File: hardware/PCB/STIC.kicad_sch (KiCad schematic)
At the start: 18 parts, among them J1 22-03-5035, J2 53047-0510, J3 53047-0310, J4 3 way molex cable, J5 Conn_01x02, U1 XIAO_BLE, U2 RM3100_Breakout, U3 OLED1_3_GND1

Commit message: More work on the BOM
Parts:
- added LASER1: Egismos Laser Module 2, symbol Graphic:SYM_LASER_Large
- U1: Manufacturer_Name (none) -> Seeed
- U2: Manufacturer_Part_Number (none) -> https://www.aliexpress.com/item/1005001698153630.html
- U3: Manufacturer_Part_Number (none) -> https://www.aliexpress.com/item/32830144222.html

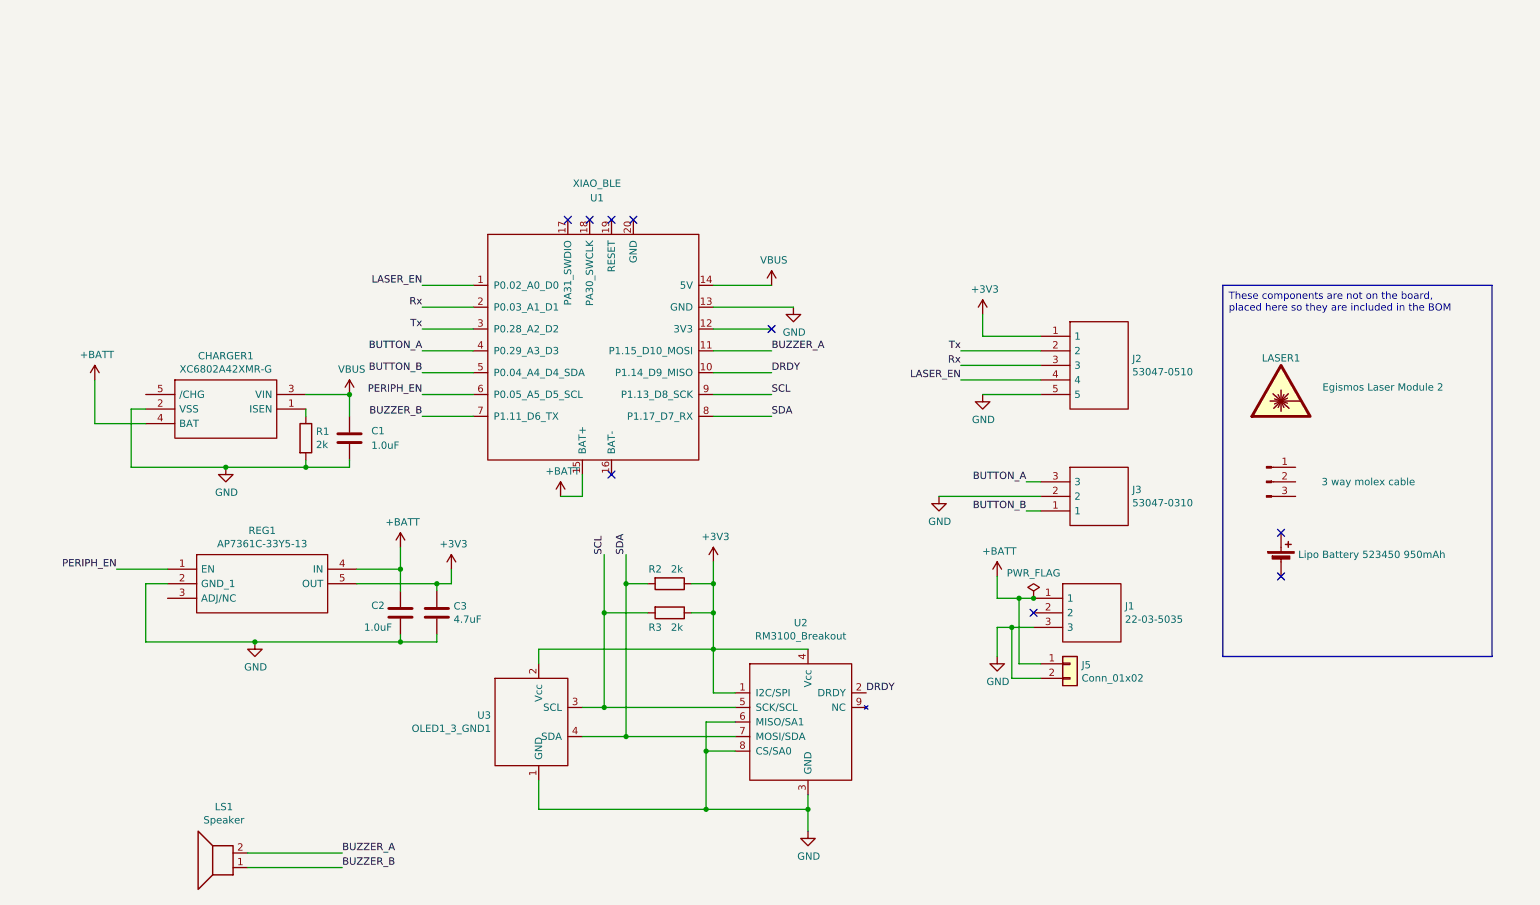
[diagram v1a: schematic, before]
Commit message: Update to Kicad v8.
Make board 5mm shorter and add SMD components
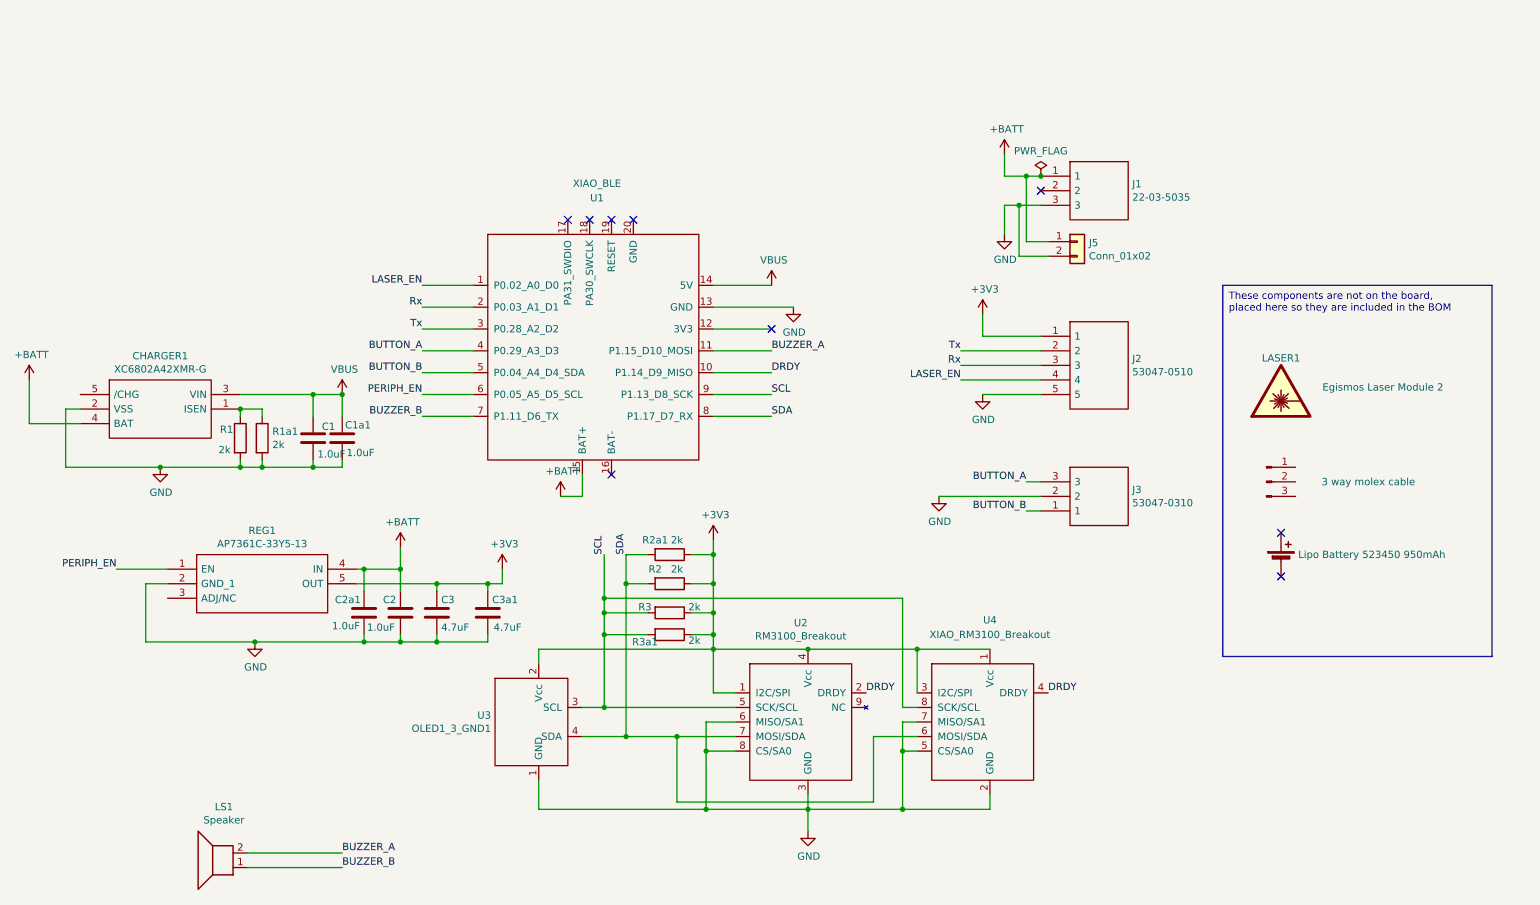
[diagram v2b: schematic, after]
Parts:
- added C1a1, C2a1: 1.0uF, Capacitor_SMD:C_0603_1608Metric, symbol Device:C
- added C3a1: 4.7uF, Capacitor_SMD:C_0603_1608Metric, symbol Device:C
- added R1a1, R2a1, R3a1: 2k, Resistor_SMD:R_0603_1608Metric, symbol Device:R
- added U4: XIAO_RM3100_Breakout, STIC:RM3100_red, symbol STIC-rescue:RM3100_red
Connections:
- net +3V3: now also C3a1.1, R2a1.1, R3a1.1, U4.1 (Vcc), U4.3 (I2C/SPI)
- net +BATT: now also C2a1.1
- net DRDY: now also U4.4 (DRDY)
- net GND: now also C1a1.2, C2a1.2, C3a1.2, R1a1.2, U4.2 (GND), U4.5 (CS/SA0), U4.7 (MISO/SA1)
- net SCL: now also R3a1.2, U4.8 (SCK/SCL)
- net SDA: now also R2a1.2, U4.6 (MOSI/SDA)
- net VBUS: now also C1a1.1
- net at CHARGER1.1 (ISEN), R1.1: now also R1a1.1
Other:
- moved on the sheet: C1, CHARGER1, J1, J5, R1

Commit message: Revert "Update to Kicad v8."
This reverts commit 377b650fb4ed8263ac52fe62880b4f170809fcf5.
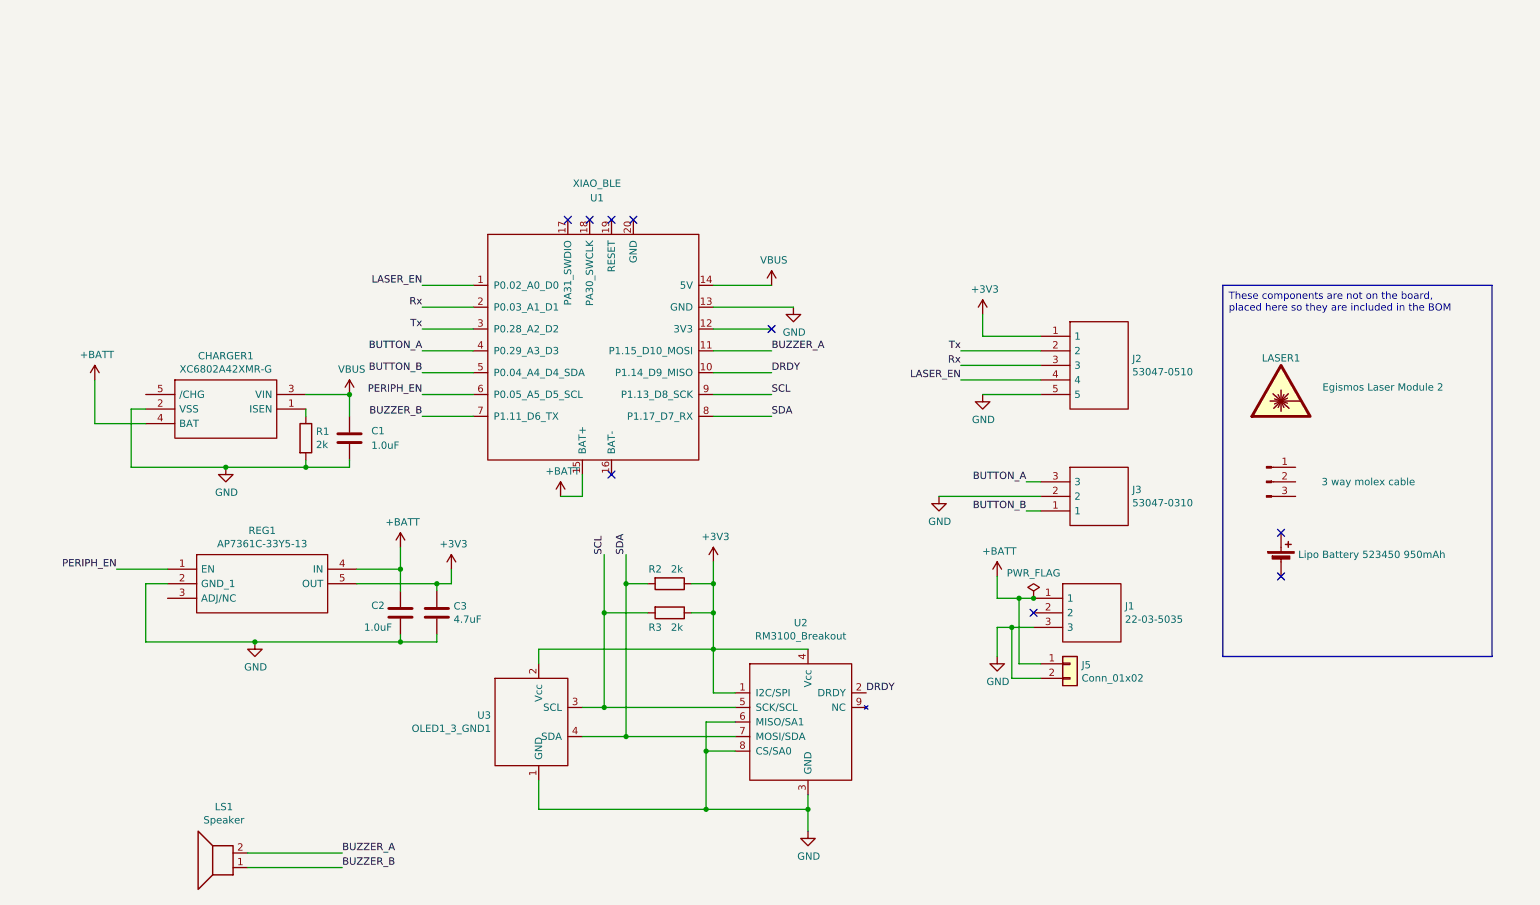
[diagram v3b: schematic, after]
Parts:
- removed C1a1, C2a1: 1.0uF, Capacitor_SMD:C_0603_1608Metric, symbol Device:C
- removed C3a1: 4.7uF, Capacitor_SMD:C_0603_1608Metric, symbol Device:C
- removed R1a1, R2a1, R3a1: 2k, Resistor_SMD:R_0603_1608Metric, symbol Device:R
- removed U4: XIAO_RM3100_Breakout, STIC:RM3100_red, symbol STIC-rescue:RM3100_red
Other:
- moved on the sheet: C1, CHARGER1, J1, J5, R1

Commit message: Merge 6.2 into main
Makes the case 5mm shorter
Also sets up "layout" system for various hardware

# Conflicts:
#	firmware/calibrate.py
#	firmware/debug.py
#	firmware/docs/source/conf.py
#	firmware/installer/installer.py
#	firmware/layouts.py
#	firmware/pins.py
#	firmware/requirements.txt
#	firmware/utils.py
#	firmware/version.py
#	firmware/versions/display128x64.py
#	hardware/Button/Button.kicad_pro
#	hardware/PCB/STIC.kicad_pcb
#	hardware/PCB/STIC.kicad_prl
#	hardware/PCB/STIC.kicad_pro
#	hardware/PCB/STIC.kicad_sch
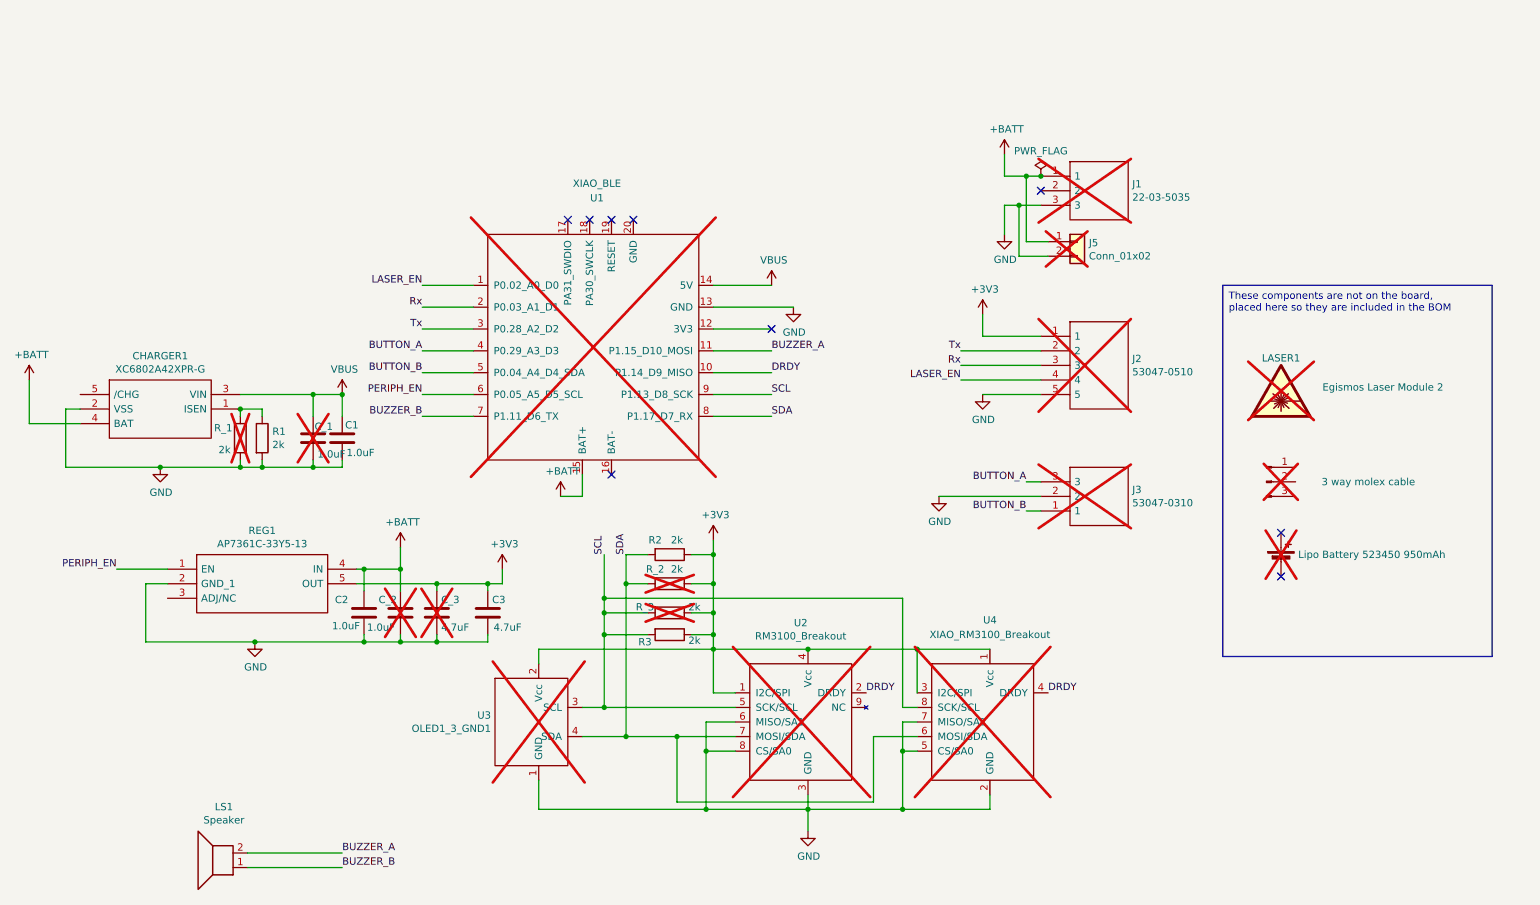
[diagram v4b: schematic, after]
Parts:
- added C1, C2: 1.0uF, Capacitor_SMD:C_0603_1608Metric, symbol Device:C
- added C3: 4.7uF, Capacitor_SMD:C_0603_1608Metric, symbol Device:C
- added R1, R2, R3: 2k, Resistor_SMD:R_0603_1608Metric, symbol Device:R
- added U4: XIAO_RM3100_Breakout, STIC:RM3100_red, symbol STIC-rescue:RM3100_red
- BT1, J1, J2, J3, J4, J5, LASER1, U1, U2, U3: now not fitted
- CHARGER1: value XC6802A42XMR-G -> XC6802A42XPR-G
- C_1: renamed from C1; now not fitted
- C_2: renamed from C2; now not fitted
- C_3: renamed from C3; now not fitted
- R_1: renamed from R1; now not fitted
- R_2: renamed from R2; now not fitted
- R_3: renamed from R3; now not fitted
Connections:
- net +3V3: now also C3.1, R2.1, R3.1, U4.1 (Vcc), U4.3 (I2C/SPI)
- net +BATT: now also C2.1
- net DRDY: now also U4.4 (DRDY)
- net GND: now also C1.2, C2.2, C3.2, R1.2, U4.2 (GND), U4.5 (CS/SA0), U4.7 (MISO/SA1)
- net SCL: now also R3.2, U4.8 (SCK/SCL)
- net SDA: now also R2.2, U4.6 (MOSI/SDA)
- net VBUS: now also C1.1
- net at CHARGER1.1 (ISEN), R_1.1: now also R1.1
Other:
- moved on the sheet: CHARGER1

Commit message: Correct part number for C1,C2
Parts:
- C1, C2: Manufacturer_Part_Number CL21B475KOFZFNE -> CL10A105KB8NNNC
- LS1: now not fitted
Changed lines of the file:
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@@
 		(in_bom yes)
 		(on_board yes)
-		(dnp no)
+		(dnp yes)
 		(property "Reference" "LS1"
 			(at 54.2798 154.5082 0)
@@
 			)
 		)
-		(property "Manufacturer_Part_Number" " CL21B475KOFZFNE "
+		(property "Manufacturer_Part_Number" "CL10A105KB8NNNC"
 			(at 74.93 90.17 0)
 			(effects
@@
 			)
 		)
-		(property "Manufacturer_Part_Number" " CL21B475KOFZFNE "
+		(property "Manufacturer_Part_Number" "CL10A105KB8NNNC"
 			(at 78.74 120.65 0)
 			(effects

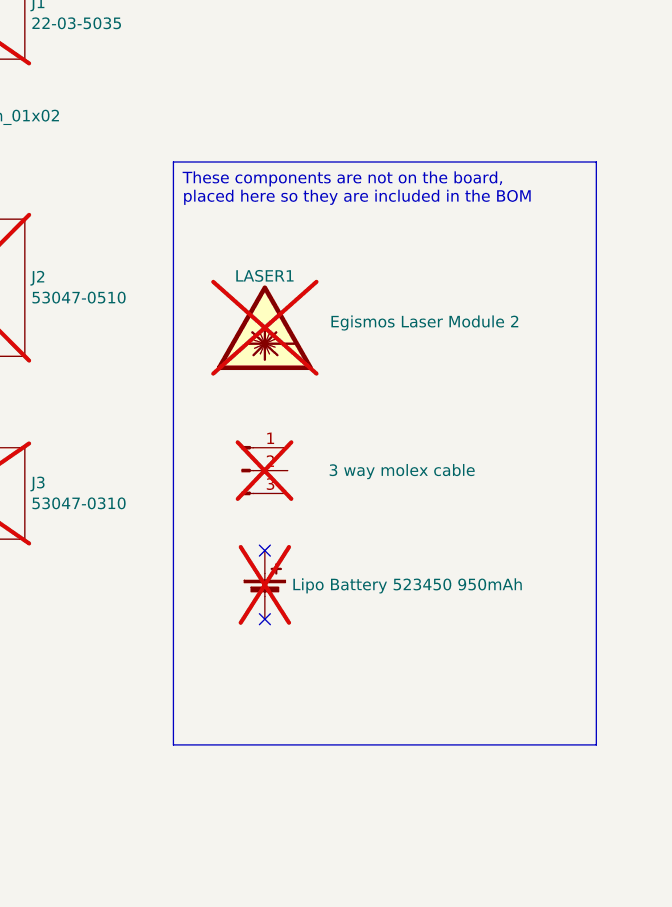
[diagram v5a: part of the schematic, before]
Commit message: update schematic so laser cable included in BOM
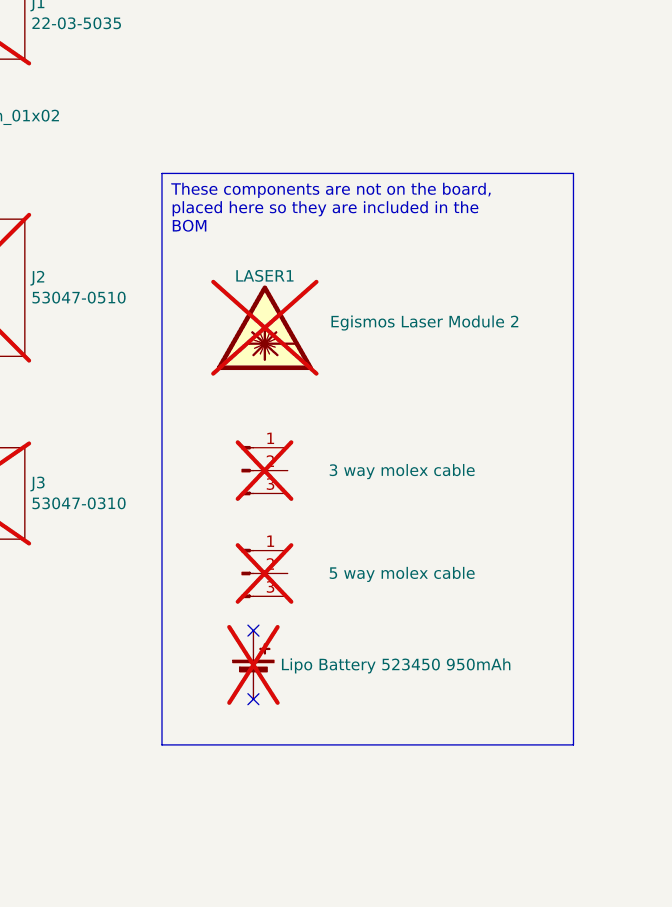
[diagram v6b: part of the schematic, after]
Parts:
- added J6: 5 way molex cable, symbol STIC-rescue:Conn_01x03_Male-Connector
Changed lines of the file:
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@@
 	)
 	(no_connect
-		(at 238.76 114.3)
+		(at 237.49 123.19)
 	)
 	(no_connect
@@
 	)
 	(no_connect
-		(at 238.76 106.68)
+		(at 237.49 115.57)
 	)
 	(no_connect
@@
 	(text_box "These components are not on the board, placed here so they are included in the BOM"
 		(exclude_from_sim no)
-		(at 228.6 63.5 0)
-		(size 46.99 64.77)
+		(at 227.33 64.77 0)
+		(size 45.72 63.5)
 		(stroke
 			(width 0)
@@
 	(symbol
 		(lib_id "Device:Battery_Cell")
-		(at 238.76 111.76 0)
+		(at 237.49 120.65 0)
 		(unit 1)
 		(exclude_from_sim no)
@@
 		(dnp yes)
 		(property "Reference" "BT1"
-			(at 241.7572 109.3216 0)
+			(at 240.4872 118.2116 0)
 			(effects
 				(font
@@
 		)
 		(property "Value" "Lipo Battery 523450 950mAh"
-			(at 241.7572 110.49 0)
+			(at 240.4872 119.38 0)
 			(effects
 				(font
@@
 		)
 		(property "Footprint" ""
-			(at 238.76 110.236 90)
+			(at 237.49 119.126 90)
 			(effects
 				(font
@@
 		)
 		(property "Datasheet" "https://cpc.farnell.com/unbranded/lp-523450-is-3/battery-lithium-pol-3-7v-950-mah/dp/BT06802"
-			(at 238.76 110.236 90)
+			(at 237.49 119.126 90)
 			(effects
 				(font
@@
 		)
 		(property "Description" "Lipo Battery 950mAh, cheaper from CPC or Amazon 523450 needed. Check polarity"
-			(at 238.76 111.76 0)
+			(at 237.49 120.65 0)
 			(effects
 				(font
@@
 		)
 		(property "Farnell Part Number" "2077888 "
-			(at 238.76 111.76 0)
+			(at 237.49 120.65 0)
 			(effects
 				(font
@@
 		)
 		(property "Manufacturer_Part_Number" "LP-523450-IS-3"
-			(at 238.76 111.76 0)
+			(at 237.49 120.65 0)
 			(effects
 				(font
@@
 		)
 		(property "LCSC Part Number" ""
-			(at 238.76 111.76 0)
+			(at 237.49 120.65 0)
 			(effects
 				(font
@@
 					(unit 1)
 				)
+			)
+		)
+	)
+	(symbol
+		(lib_id "STIC-rescue:Conn_01x03_Male-Connector")
+		(at 236.22 109.22 0)
+		(unit 1)
+		(exclude_from_sim no)
+		(in_bom yes)
+		(on_board no)
+		(dnp yes)
+		(property "Reference" "J6"
+			(at 238.9632 102.0826 0)
+			(effects
+				(font
+					(size 1.27 1.27)
+				)
+				(hide yes)
+			)
+		)
+		(property "Value" "5 way molex cable"
+			(at 254 109.22 0)
+			(effects
+				(font
+					(size 1.27 1.27)
+				)
+			)
+		)
+		(property "Footprint" ""
+			(at 236.22 109.22 0)
+			(effects
+				(font
+					(size 1.27 1.27)
+				)
+				(hide yes)
+			)
+		)
+		(property "Datasheet" "~"
+			(at 236.22 109.22 0)
+			(effects
+				(font
+					(size 1.27 1.27)
+				)
+				(hide yes)
+			)
+		)
+		(property "Description" ""
+			(at 236.22 109.22 0)
+			(effects
+				(font
+					(size 1.27 1.27)
+				)
+				(hide yes)
+			)
+		)
+		(property "Farnell Part Number" "2671462 "
+			(at 236.22 109.22 0)
+			(effects
+				(font
+					(size 1.27 1.27)
+				)
+				(hide yes)
+			)
+		)
+		(property "Manufacturer_Part_Number" "15134-0500"
+			(at 236.22 109.22 0)
+			(effects
+				(font
+					(size 1.27 1.27)
+				)
+				(hide yes)
+			)
+		)
+		(property "LCSC Part Number" ""
+			(at 236.22 109.22 0)
+			(effects
+				(font
+					(size 1.27 1.27)
+				)
+				(hide yes)
+			)
+		)
+		(pin "3"
+		)
+		(pin "2"
+		)
+		(pin "1"
+		)
+		(instances
+			(project "STIC"
+				(path "/9d05c150-179f-4a8a-bd17-6d3f46b64a83"
+					(reference "J6")
+					(unit 1)
+				)
